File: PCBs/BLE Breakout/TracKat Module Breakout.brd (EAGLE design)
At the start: 29.2 x 88.9 mm, 16 parts, among them J1 TC2030-CTX-NL, U1 DA14531MOD-00F01002, X2 22-23-2021

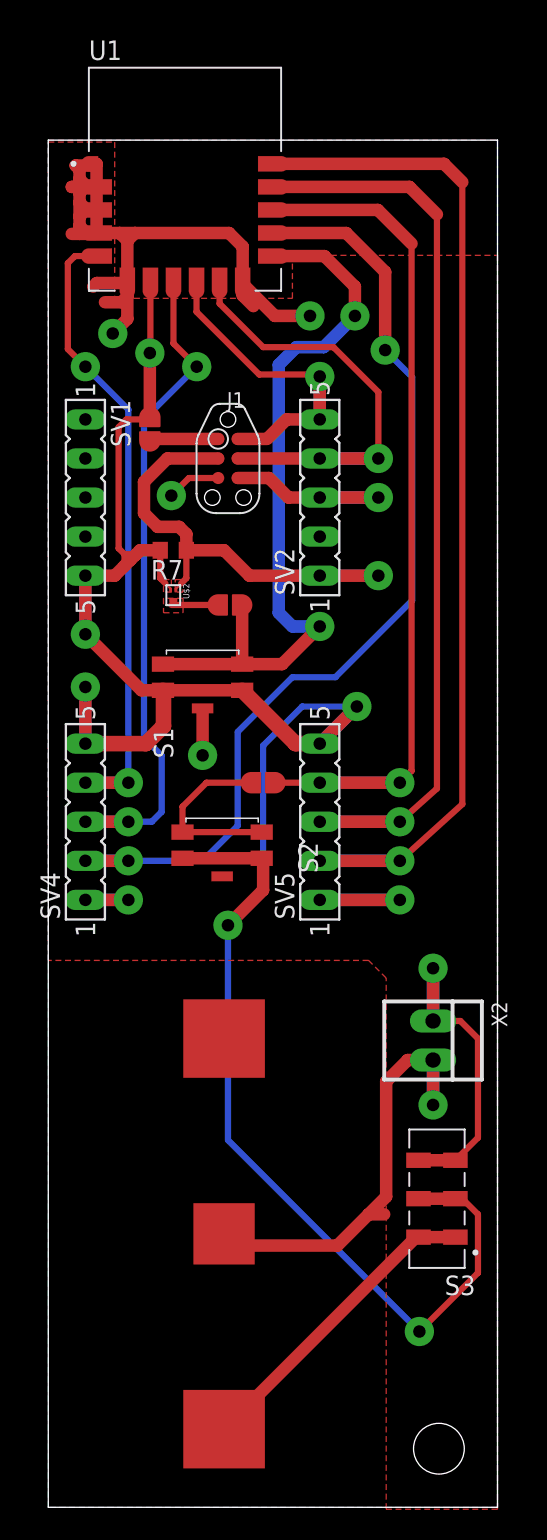
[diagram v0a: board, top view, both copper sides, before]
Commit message: Improve routing and copper pour isolation
This design is fully functional but still has two errors: 1) SWD V_ref is placed on bottom pin of top left header - this should be routed to top pin instead 2) Middle and lower copper pours on bottom layer are isolated and must have GND jumped to them
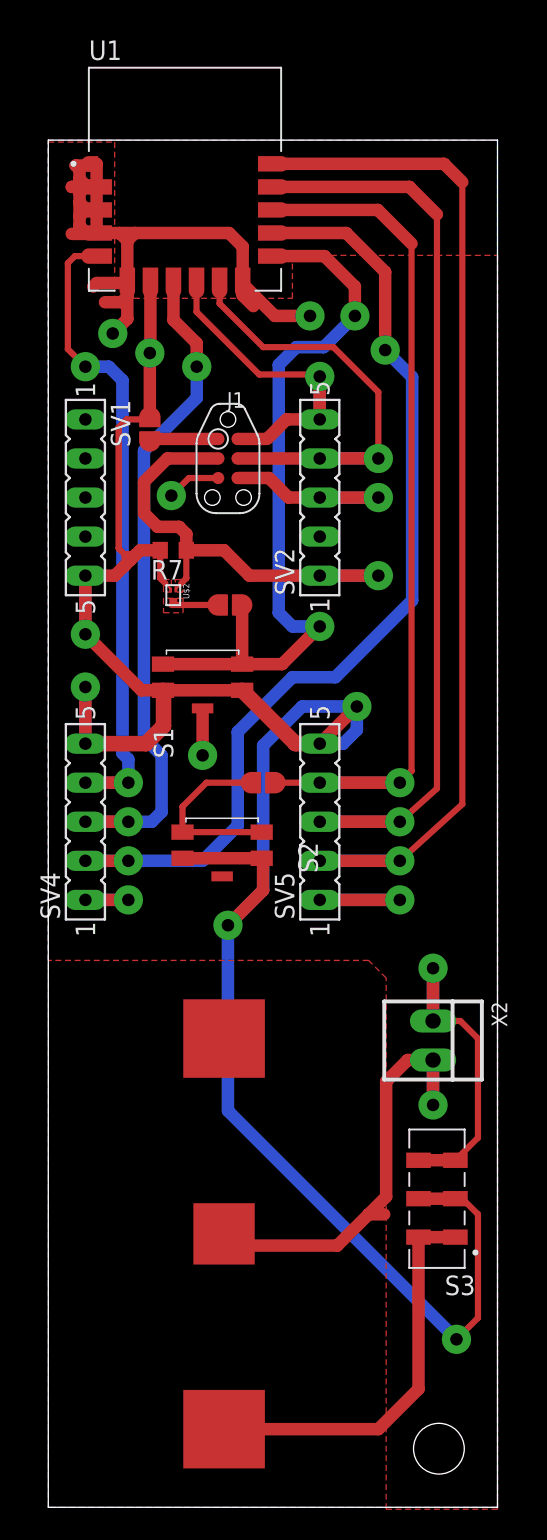
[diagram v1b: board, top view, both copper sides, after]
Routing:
- net V_BATT: track 21.6 -> 27.4 mm
- net V_HIGH: track 153.3 -> 155.2 mm
- net GPIO_1: track 43.1 -> 44.0 mm
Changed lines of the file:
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@@
 <via x="5.207" y="39.497" extent="1-16" drill="0.8128" diameter="1.905"/>
 <wire x1="5.207" y1="39.497" x2="2.413" y2="39.497" width="0.8128" layer="16"/>
-<polygon width="0.8128" layer="16">
+<polygon width="0.8128" layer="16" isolate="0.8128">
 <vertex x="0" y="88.9"/>
 <vertex x="29.21" y="88.9"/>
@@
 <wire x1="12.64" y1="78.8" x2="13.335" y2="78.105" width="0.8128" layer="1"/>
 <wire x1="5.207" y1="39.497" x2="11.303" y2="41.028" width="0" layer="19" extent="1-1"/>
+<wire x1="10.033" y1="48.895" x2="11.303" y2="41.028" width="0" layer="19" extent="1-1"/>
 </signal>
 <signal name="V_HIGH">
@@
 <via x="6.604" y="75.057" extent="1-16" drill="0.8128" diameter="1.905"/>
 <wire x1="6.604" y1="75.057" x2="6.64" y2="75.093" width="0.4064" layer="1"/>
-<wire x1="6.64" y1="79.61" x2="6.64" y2="75.093" width="0.4064" layer="1"/>
+<wire x1="6.64" y1="79.61" x2="6.64" y2="75.093" width="0.8128" layer="1"/>
 <wire x1="6.64" y1="75.093" x2="6.64" y2="74.839" width="0.4064" layer="1"/>
 <wire x1="2.413" y1="60.579" x2="2.413" y2="56.769" width="0.8128" layer="1"/>
@@
 <wire x1="17.653" y1="49.657" x2="20.066" y2="52.07" width="0.8128" layer="1"/>
 <via x="20.066" y="52.07" extent="1-16" drill="0.8128" diameter="1.905"/>
-<wire x1="20.066" y1="52.07" x2="17.653" y2="49.657" width="0.8128" layer="16"/>
+<wire x1="20.066" y1="50.546" x2="19.177" y2="49.657" width="0.8128" layer="16"/>
+<wire x1="19.177" y1="49.657" x2="17.653" y2="49.657" width="0.8128" layer="16"/>
+<wire x1="20.066" y1="52.07" x2="20.066" y2="50.546" width="0.8128" layer="16"/>
 <wire x1="8.728" y1="42.203" x2="13.878" y2="42.203" width="0.8128" layer="1"/>
 <wire x1="13.878" y1="42.203" x2="13.97" y2="42.111" width="0.8128" layer="1"/>
 <wire x1="13.97" y1="42.111" x2="13.97" y2="40.132" width="0.8128" layer="1"/>
 <wire x1="26.473" y1="20.066" x2="24.073" y2="20.066" width="0.8128" layer="1"/>
-<wire x1="20.066" y1="52.07" x2="16.51" y2="52.07" width="0.4064" layer="16"/>
-<wire x1="16.51" y1="52.07" x2="13.97" y2="49.53" width="0.4064" layer="16"/>
-<wire x1="13.97" y1="49.53" x2="13.97" y2="40.132" width="0.4064" layer="16"/>
+<wire x1="20.066" y1="52.07" x2="16.51" y2="52.07" width="0.8128" layer="16"/>
+<wire x1="16.51" y1="52.07" x2="13.97" y2="49.53" width="0.8128" layer="16"/>
+<wire x1="13.97" y1="49.53" x2="13.97" y2="40.132" width="0.8128" layer="16"/>
 <via x="11.684" y="37.846" extent="1-16" drill="0.8128" diameter="1.905"/>
-<wire x1="13.97" y1="40.132" x2="11.684" y2="37.846" width="0.4064" layer="16"/>
-<wire x1="11.684" y1="37.846" x2="11.684" y2="23.876" width="0.4064" layer="16"/>
-<wire x1="11.684" y1="23.876" x2="24.13" y2="11.43" width="0.4064" layer="16"/>
-<via x="24.13" y="11.43" extent="1-16" drill="0.8128" diameter="1.905"/>
-<wire x1="24.13" y1="11.43" x2="27.94" y2="15.24" width="0.4064" layer="1"/>
-<wire x1="27.94" y1="15.24" x2="27.94" y2="19.05" width="0.4064" layer="1"/>
+<wire x1="13.97" y1="40.132" x2="11.684" y2="37.846" width="0.8128" layer="16"/>
+<wire x1="11.684" y1="37.846" x2="11.684" y2="25.781" width="0.8128" layer="16"/>
+<wire x1="11.684" y1="25.781" x2="26.543" y2="10.922" width="0.8128" layer="16"/>
+<via x="26.543" y="10.922" extent="1-16" drill="0.8128" diameter="1.905"/>
+<wire x1="26.543" y1="10.922" x2="27.94" y2="12.319" width="0.4064" layer="1"/>
+<wire x1="27.94" y1="12.319" x2="27.94" y2="19.05" width="0.4064" layer="1"/>
 <wire x1="27.94" y1="19.05" x2="26.924" y2="20.066" width="0.4064" layer="1"/>
 <wire x1="26.924" y1="20.066" x2="26.473" y2="20.066" width="0.4064" layer="1"/>
@@
 <wire x1="11.43" y1="30.48" x2="12.406" y2="31.456" width="0.8128" layer="1"/>
 <wire x1="26.473" y1="17.566" x2="24.073" y2="17.566" width="0.8128" layer="1"/>
-<wire x1="11.43" y1="5.08" x2="23.916" y2="17.566" width="0.8128" layer="1"/>
-<wire x1="23.916" y1="17.566" x2="24.073" y2="17.566" width="0.8128" layer="1"/>
+<wire x1="11.43" y1="5.08" x2="21.463" y2="5.08" width="0.8128" layer="1"/>
+<wire x1="21.463" y1="5.08" x2="24.073" y2="7.69" width="0.8128" layer="1"/>
+<wire x1="24.073" y1="7.69" x2="24.073" y2="17.566" width="0.8128" layer="1"/>
 <wire x1="24.073" y1="17.566" x2="11.43" y2="30.48" width="0" layer="19" extent="1-1"/>
 </signal>
@@
 <wire x1="1.27" y1="75.311" x2="2.413" y2="74.168" width="0.4064" layer="1"/>
 <via x="2.413" y="74.168" extent="1-16" drill="0.8128" diameter="1.905"/>
-<wire x1="2.413" y1="74.168" x2="5.207" y2="71.374" width="0.4064" layer="16"/>
+<wire x1="4.826" y1="73.279" x2="3.937" y2="74.168" width="0.8128" layer="16"/>
+<wire x1="2.413" y1="74.168" x2="3.937" y2="74.168" width="0.8128" layer="16"/>
 <via x="5.207" y="47.117" extent="1-16" drill="0.8128" diameter="1.905"/>
-<wire x1="5.207" y1="71.374" x2="5.207" y2="47.117" width="0.4064" layer="16"/>
 <wire x1="2.413" y1="47.117" x2="5.207" y2="47.117" width="0.8128" layer="1"/>
 <wire x1="2.413" y1="47.117" x2="5.207" y2="47.117" width="0.8128" layer="16"/>
+<wire x1="5.207" y1="47.117" x2="5.207" y2="48.641" width="0.8128" layer="16"/>
+<wire x1="5.207" y1="48.641" x2="4.826" y2="49.022" width="0.8128" layer="16"/>
+<wire x1="4.826" y1="49.022" x2="4.826" y2="73.279" width="0.8128" layer="16"/>
 </signal>
 <signal name="GPIO_3">
@@
 <wire x1="5.207" y1="42.037" x2="2.413" y2="42.037" width="0.8128" layer="1"/>
 <via x="21.9075" y="75.2475" extent="1-16" drill="0.8128" diameter="1.905"/>
-<wire x1="21.9075" y1="75.2475" x2="23.6601" y2="73.4949" width="0.4064" layer="16"/>
-<wire x1="23.6601" y1="73.4949" x2="23.6601" y2="58.9661" width="0.4064" layer="16"/>
-<wire x1="23.6601" y1="58.9661" x2="18.669" y2="53.975" width="0.4064" layer="16"/>
-<wire x1="12.319" y1="44.323" x2="10.033" y2="42.037" width="0.4064" layer="16"/>
-<wire x1="10.033" y1="42.037" x2="5.207" y2="42.037" width="0.4064" layer="16"/>
-<wire x1="18.669" y1="53.975" x2="15.875" y2="53.975" width="0.4064" layer="16"/>
-<wire x1="12.319" y1="50.419" x2="12.319" y2="44.323" width="0.4064" layer="16"/>
-<wire x1="15.875" y1="53.975" x2="12.319" y2="50.419" width="0.4064" layer="16"/>
+<wire x1="21.9075" y1="75.2475" x2="23.6601" y2="73.4949" width="0.8128" layer="16"/>
+<wire x1="23.6601" y1="73.4949" x2="23.6601" y2="58.9661" width="0.8128" layer="16"/>
+<wire x1="23.6601" y1="58.9661" x2="18.669" y2="53.975" width="0.8128" layer="16"/>
+<wire x1="12.319" y1="44.323" x2="10.033" y2="42.037" width="0.8128" layer="16"/>
+<wire x1="10.033" y1="42.037" x2="5.207" y2="42.037" width="0.8128" layer="16"/>
+<wire x1="18.669" y1="53.975" x2="15.875" y2="53.975" width="0.8128" layer="16"/>
+<wire x1="12.319" y1="50.419" x2="12.319" y2="44.323" width="0.8128" layer="16"/>
+<wire x1="15.875" y1="53.975" x2="12.319" y2="50.419" width="0.8128" layer="16"/>
 </signal>
 <signal name="GPIO_2">
 <contactref element="U1" pad="J8"/>
 <contactref element="SV4" pad="3"/>
-<wire x1="8.14" y1="79.61" x2="8.14" y2="75.68" width="0.4064" layer="1"/>
+<wire x1="8.14" y1="79.61" x2="8.14" y2="77.204" width="0.8128" layer="1"/>
 <via x="9.652" y="74.168" extent="1-16" drill="0.8128" diameter="1.905"/>
-<wire x1="8.14" y1="75.68" x2="9.652" y2="74.168" width="0.4064" layer="1"/>
+<wire x1="9.652" y1="75.692" x2="8.14" y2="77.204" width="0.8128" layer="1"/>
+<wire x1="9.652" y1="75.692" x2="9.652" y2="74.168" width="0.8128" layer="1"/>
 <wire x1="2.413" y1="44.577" x2="5.207" y2="44.577" width="0.8128" layer="1"/>
 <via x="5.207" y="44.577" extent="1-16" drill="0.8128" diameter="1.905"/>
-<wire x1="5.207" y1="44.577" x2="6.731" y2="44.577" width="0.4064" layer="16"/>
-<wire x1="7.366" y1="45.212" x2="6.731" y2="44.577" width="0.4064" layer="16"/>
-<wire x1="6.223" y1="70.739" x2="9.652" y2="74.168" width="0.4064" layer="16"/>
-<wire x1="7.366" y1="48.895" x2="7.366" y2="45.212" width="0.4064" layer="16"/>
-<wire x1="6.223" y1="50.038" x2="6.223" y2="70.739" width="0.4064" layer="16"/>
-<wire x1="6.223" y1="50.038" x2="7.366" y2="48.895" width="0.4064" layer="16"/>
+<wire x1="5.207" y1="44.577" x2="6.731" y2="44.577" width="0.8128" layer="16"/>
+<wire x1="7.366" y1="45.212" x2="6.731" y2="44.577" width="0.8128" layer="16"/>
+<wire x1="9.652" y1="72.136" x2="6.223" y2="68.707" width="0.8128" layer="16"/>
+<wire x1="9.652" y1="72.136" x2="9.652" y2="74.168" width="0.8128" layer="16"/>
+<wire x1="7.366" y1="48.895" x2="7.366" y2="45.212" width="0.8128" layer="16"/>
+<wire x1="6.223" y1="50.038" x2="6.223" y2="68.707" width="0.8128" layer="16"/>
+<wire x1="6.223" y1="50.038" x2="7.366" y2="48.895" width="0.8128" layer="16"/>
 <wire x1="2.413" y1="44.577" x2="5.207" y2="44.577" width="0.8128" layer="16"/>
 </signal>
